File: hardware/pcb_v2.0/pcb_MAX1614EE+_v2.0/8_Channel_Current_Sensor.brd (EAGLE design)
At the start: 31.8 x 36.8 mm, 45 parts, among them Q1 BSS138, Q2 BSS138, SW1 DIP-SLIDE-SWITCH-EG1218

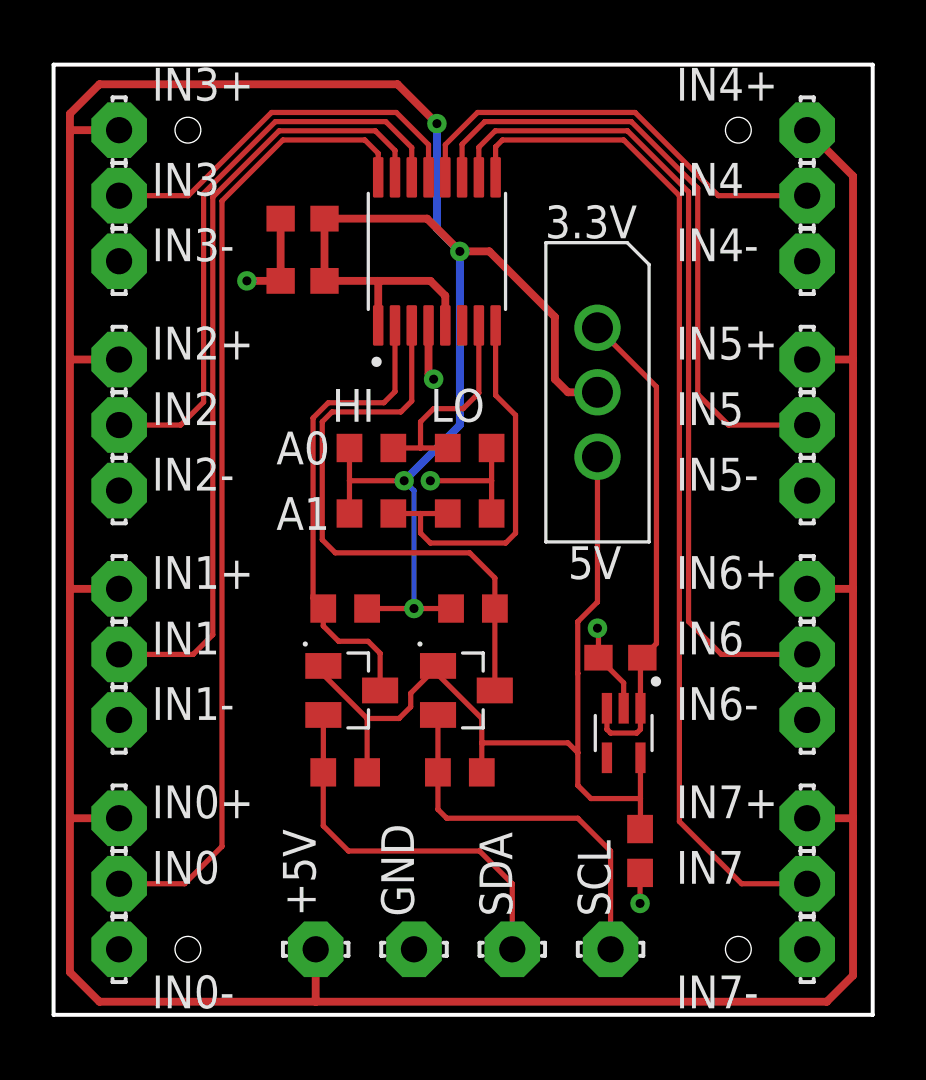
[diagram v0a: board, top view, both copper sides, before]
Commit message: New PCB designs, reorganized files, removed clutter
Added pcb v1.2 the final draft of the ADC12818 board.
Added pcb v2.0 the new board boased on the MAX1614EE+ ADC
Added datasheet for MAX ADC
Renamed folders to have consistent naming scheme
Removed unncessary tempoary files
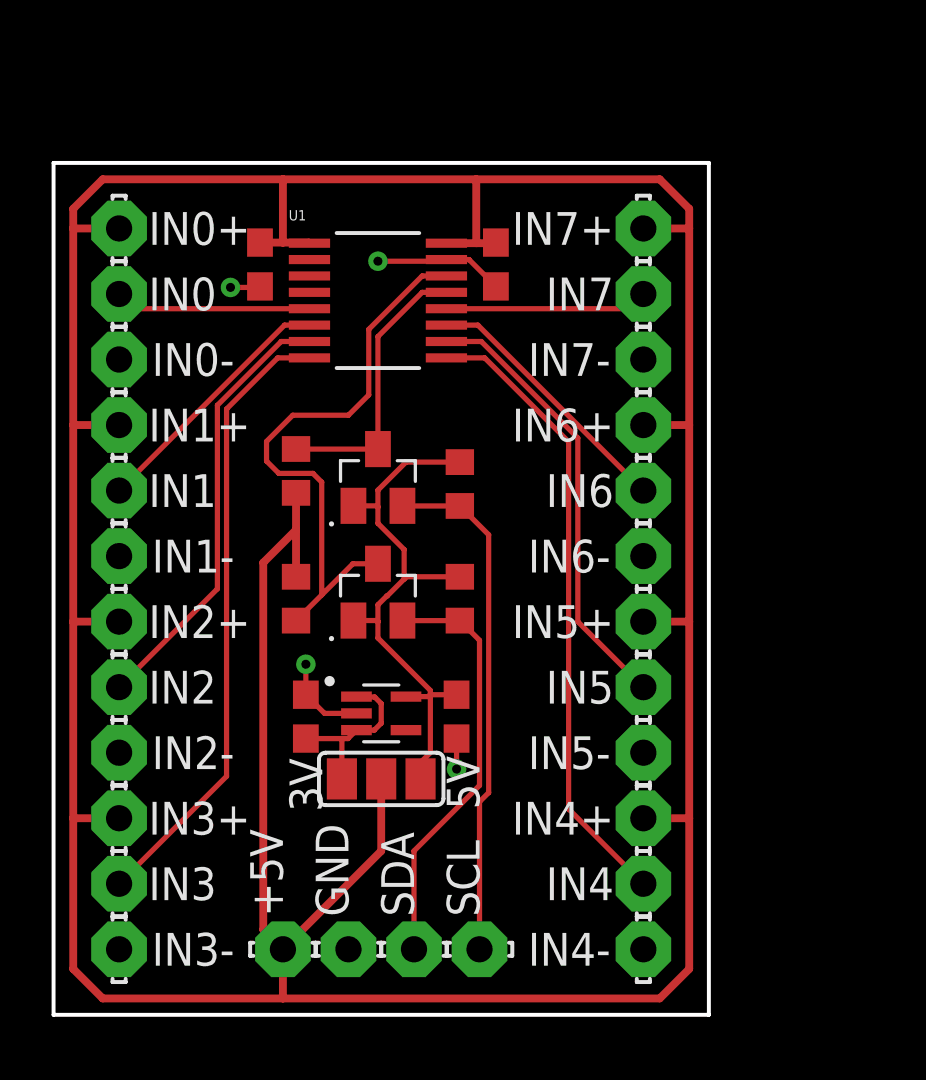
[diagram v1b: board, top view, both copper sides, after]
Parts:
- removed ADC: ADC128D818CIMT/NOPB, ADC128D818CIMT_NOPB:SOP65P640X120-16N
- removed C1: .1uF, resistor:C0603
- removed C2, C3, C5: 1uF, resistor:C0603
- removed R1, R2, R3, R4, R5, R6, R7, R8: 10k, resistor:R0603
- removed SW1: DIP-SLIDE-SWITCH-EG1218, EG1218-DIP-SLIDE-SWITCH:SW3-2.5-11.6X4.0X5.4+2.0MM
- added +5V_JUMP: (no value), jumper:SJ_2
- added CARB, CASB: 0.1uF, resistor:C0603
- added CROB, CRSB: 1uF, resistor:C0603
- added RC3, RC5, RD3, RD5: 10k, resistor:R0603
- added U1: MAX11614EEET, MAX11614EEET:21-0055H_16
- moved IN4 27.4 mm to (22.9, 5.08)
- moved IN4- 27.4 mm to (22.9, 2.54)
- moved IN4+ 27.4 mm to (22.9, 7.62)
- moved IN3 26.7 mm to (2.54, 5.08)
- moved IN3- 26.7 mm to (2.54, 2.54)
- moved IN3+ 26.7 mm to (2.54, 7.62)
- moved IN7 23.7 mm to (22.9, 27.9)
- moved IN7+ 23.7 mm to (22.9, 30.5)
- moved IN7- 23.7 mm to (22.9, 25.4)
- moved IN0 22.9 mm to (2.54, 27.9)
- moved IN0+ 22.9 mm to (2.54, 30.5)
- moved IN0- 22.9 mm to (2.54, 25.4)
- moved IN5 12.0 mm to (22.9, 12.7)
- moved IN5- 12.0 mm to (22.9, 10.2)
- moved IN5+ 12.0 mm to (22.9, 15.2)
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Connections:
- removed net +5V-S: C5.1, REG.1, REG.3, SW1.1
- removed net A0: ADC.7, R1.1, R2.2
- removed net A1: ADC.8, R3.1, R4.2
- removed net INT: ADC.6
- new net +5V-R: +5V_JUMP.3, CRSB.1, REG.1, REG.3
- net +5V: now also +5V_JUMP.2, CARB.1, CASB.1, RC5.1, RD5.1, U1.1, U1.16; no longer ADC.1, ADC.5, C1.1, C2.1, R1.2, R3.2, R7.1, R8.1, SW1.2
- net GND: now also CARB.2, CASB.2, CROB.2, CRSB.2, U1.15; no longer ADC.4, C1.2, C2.2, C3.2, C5.2, R2.1, R4.1
- net IN0: now also U1.5; no longer ADC.16
- net IN1: now also U1.6; no longer ADC.15
- net IN2: now also U1.7; no longer ADC.14
- net IN3: now also U1.8; no longer ADC.13
- net IN4: now also U1.9; no longer ADC.12
- net IN5: now also U1.10; no longer ADC.11
- net IN6: now also U1.11; no longer ADC.10
- net IN7: now also U1.12; no longer ADC.9
- net SCL: now also RC3.1; no longer R5.1
- net SCL5: now also RC5.2, U1.13; no longer ADC.3, R7.2
- net SDA: now also RD3.1; no longer R6.1
- net SDA5: now also RD5.2, U1.14; no longer ADC.2, R8.2
- net V-PU: now also +5V_JUMP.1, CROB.1, RC3.2, RD3.2; no longer C3.1, R5.2, R6.2, SW1.3
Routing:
- net IN7: track 39.5 -> 7.87 mm
- net IN0: track 37.8 -> 7.62 mm
- net IN6: track 32.3 -> 10.3 mm
- net IN1: track 30.4 -> 10.0 mm
- net +5V: track 182.1 -> 162.0 mm, vias 4 -> 0
- net +5V-S: track 19.1 -> 0.00 mm
- net A1: track 15.2 -> 0.00 mm
- net V-PU: track 36.0 -> 22.8 mm
- net SCL5: track 23.0 -> 10.9 mm
- net IN3: track 15.1 -> 24.2 mm
- net A0: track 8.50 -> 0.00 mm
- net IN4: track 17.1 -> 24.4 mm
- net IN5: track 24.6 -> 17.4 mm
- net +5V-R: track 0.00 -> 6.56 mm
- net IN2: track 22.5 -> 17.1 mm
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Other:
- board size 31.8 x 36.8 mm -> 25.4 x 33 mm
- board text added: "3V"
- board text removed: "3.3V"
- board text removed: "A0"
- board text removed: "A1"
- board text removed: "HI"
- board text removed: "LO"

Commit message: Finished v2 of ADC board
Completed changes to ADC board and parts list.
Changes:
-Added header for voltage directly from the battery
-Added voltage divider to measure battery voltage
-Added buck converter to make clean 5V from battery voltage
-Switched to more accurate MAX1614 ADC
-Rearranged components and added solder jumpers as appropriate
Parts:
- removed +5V: LSP10, solpad:LSP10
- removed +5V_JUMP: (no value), jumper:SJ_2
- removed REG: LD59015C33R, LD59015C33R:SOT65P210X110-5N
- added 3V3REG: LD59015C33R, LD59015C33R:SOT65P210X110-5N
- added 5VBUCK: ACT4088US-T, ACT4088US-T:SOT236
- added C1: 10uF, resistor:C0603K
- added C2, C3: 22uF, resistor:C0603K
- added CVD: 0.1uF, resistor:C0603K
- added D1: NSR20F30NXT5G, NSR20F30NXT5G:C0603K
- added G, V+, VCC: LSP10, solpad:LSP10
- added JUMP_+5V, JUMP_CH0, JUMP_VI2C: (no value), jumper:SJ_2
- added L1: 4.7uF, rc-master-smd:PM1008
- added RDV2, RFB2: 9.65k, resistor:R0603
- added RFB1, RVD1: 49.9k, resistor:R0603
- moved CROB 5.90 mm to (17.5, 17.1)
- moved CRSB 5.90 mm to (11.7, 17.1)
- moved RC5 4.95 mm to (11.3, 25.7)
- moved RD5 4.95 mm to (11.3, 20.7)
- moved Q1 4.95 mm to (14.5, 25.4)
- moved Q2 4.95 mm to (14.5, 21.0)
- moved RC3 4.95 mm to (17.7, 25.1)
- moved RD3 4.95 mm to (17.7, 20.7)
- moved CARB 2.84 mm to (8.51, 31.9)
- moved CASB 2.84 mm to (17.7, 31.9)
- moved U1 2.84 mm to (13.1, 30.5)
- moved IN4 0.25 mm to (22.6, 5.08)
- moved IN4+ 0.25 mm to (22.6, 7.62)
- moved IN4- 0.25 mm to (22.6, 2.54)
- moved IN5 0.25 mm to (22.6, 12.7)
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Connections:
- new net BST: 5VBUCK.6, C3.2
- new net CH0: JUMP_CH0.2, U1.5
- new net FB: 5VBUCK.4, RFB1.1, RFB2.2
- new net IN: 5VBUCK.2, C1.1, RVD1.2, V+.MP
- new net SW: 5VBUCK.1, C3.1, D1.2, L1.2
- new net VCC: JUMP_+5V.3, VCC.MP
- new net VD: CVD.1, JUMP_CH0.3, RDV2.2, RVD1.1
- new net VR+: C2.1, JUMP_+5V.1, L1.1, RFB1.2
- net +5V: now also JUMP_+5V.2, JUMP_VI2C.2; no longer +5V.MP, +5V_JUMP.2
- net +5V-R: now also 3V3REG.1, 3V3REG.3, JUMP_VI2C.3; no longer +5V_JUMP.3, REG.1, REG.3
- net GND: now also 3V3REG.2, 5VBUCK.5, C1.2, C2.2, CVD.2, D1.1, G.MP, RDV2.1, RFB2.1; no longer REG.2
- net IN0: now also JUMP_CH0.1; no longer U1.5
- net NC: now also 3V3REG.4; no longer REG.4
- net V-PU: now also 3V3REG.5, JUMP_VI2C.1; no longer +5V_JUMP.1, REG.5
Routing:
- net GND: track 10.9 -> 37.0 mm, vias 4 -> 5
- net VD: track 0.00 -> 23.5 mm, vias 0 -> 2
- net VR+: track 0.00 -> 18.7 mm
- net IN1: track 10.0 -> 27.1 mm
- net CH0: track 0.00 -> 12.0 mm
- net SDA: track 16.3 -> 25.7 mm
- net SCL: track 20.0 -> 29.0 mm
- net IN: track 0.00 -> 6.91 mm
- net IN2: track 17.1 -> 23.4 mm
- net SW: track 0.00 -> 5.63 mm
- net FB: track 0.00 -> 4.79 mm
- net IN3: track 24.2 -> 28.7 mm
- net +5V: track 162.0 -> 166.0 mm
- net IN6: track 10.3 -> 14.1 mm
- net IN4: track 24.4 -> 28.3 mm
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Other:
- board size 25.4 x 33 mm -> 25.1 x 34.3 mm
- board text added: "GND"
- board text added: "IN0"
- board text added: "SCL"
- board text added: "SDA"
- board text added: "VCC"
- board text added: "VD"
- board text added: "VR+"
